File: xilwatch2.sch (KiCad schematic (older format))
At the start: 31 parts, among them J1 Conn_SWD, M1 Vibrator, Q1 NTR5103N, SW1 Btn_Up, SW2 Btn_Down, SW3 Btn_Select, SW4 Btn_Back, U1 ATSAMD21J18A-MU

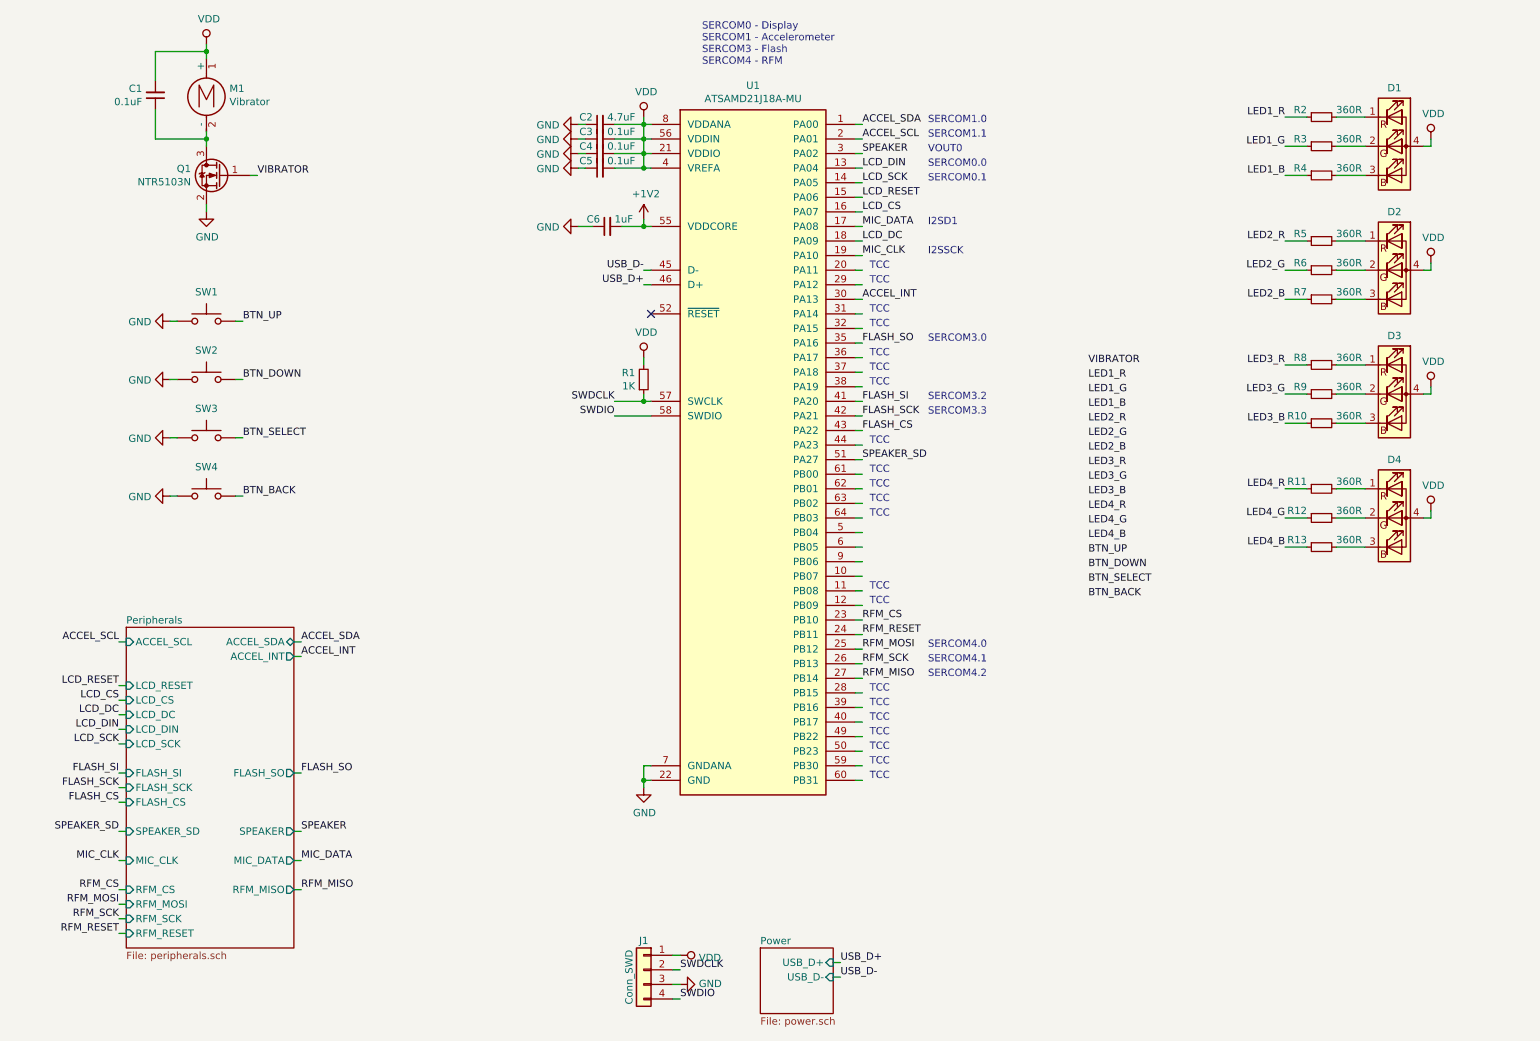
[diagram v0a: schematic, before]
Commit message: Change of plans, now a nRF52840 with E-ink
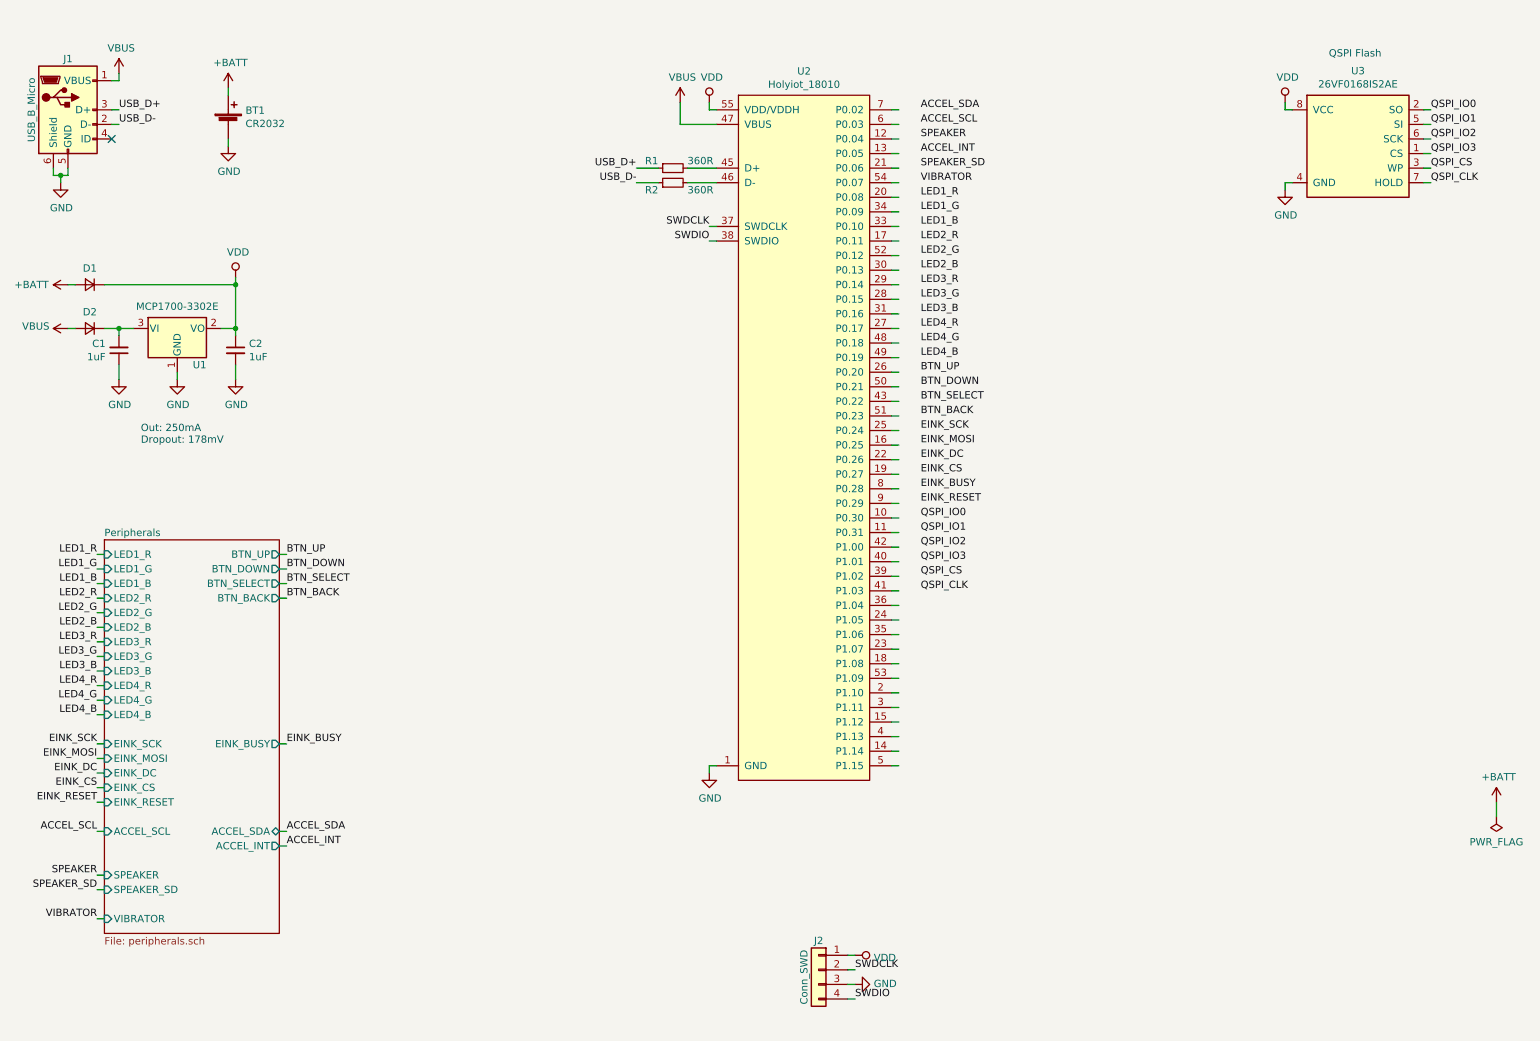
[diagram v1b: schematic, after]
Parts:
- removed C3, C4, C5: 0.1uF, Capacitor_SMD:C_0603_1608Metric, symbol Device:C_Small
- removed C6: 1uF, Capacitor_SMD:C_0603_1608Metric, symbol Device:C_Small
- removed D1: LED_TopLeft, LED_SMD_Extra:LED_RGBA_0606, symbol Device_Extra:LED_RGBA
- removed D2: LED_TopRight, LED_SMD_Extra:LED_RGBA_0606, symbol Device_Extra:LED_RGBA
- removed D3: LED_BottomLeft, LED_SMD_Extra:LED_RGBA_0606, symbol Device_Extra:LED_RGBA
- removed D4: LED_BottomRight, LED_SMD_Extra:LED_RGBA_0606, symbol Device_Extra:LED_RGBA
- removed M1: Vibrator, Buzzer_Beeper_Extra:C1026B, symbol Motor:Motor_DC
- removed Q1: NTR5103N, Package_TO_SOT_SMD:SOT-23, symbol Transistor_FET:BSS138
- removed R10, R11, R12, R13, R3, R4, R5, R6, R7, R8, R9: 360R, Resistor_SMD:R_0603_1608Metric, symbol Device:R_Small
- removed SW1: Btn_Up, Button_Switch_SMD_Extra:KLS7-TS2402, symbol Switch:SW_Push
- removed SW2: Btn_Down, Button_Switch_SMD_Extra:KLS7-TS2402, symbol Switch:SW_Push
- removed SW3: Btn_Select, Button_Switch_SMD_Extra:KLS7-TS2402, symbol Switch:SW_Push
- removed SW4: Btn_Back, Button_Switch_SMD_Extra:KLS7-TS2402, symbol Switch:SW_Push
- removed U1: ATSAMD21J18A-MU, Package_DFN_QFN:QFN-64-1EP_9x9mm_P0.5mm_EP4.7x4.7mm, symbol MCU_Microchip_SAMD:ATSAMD21J18A-MU
- added BT1: CR2032, Battery_Extra:BAT-HLD-001, symbol Device:Battery_Cell
- added D1, D2: S1JHE, Diode_SMD:D_SOD-323F, symbol Device:D_Small
- added J1: USB_B_Micro, Connector_USB:USB_Micro-B_Molex-105017-0001, symbol Connector:USB_B_Micro
- added U1: MCP1700-3302E, Package_TO_SOT_SMD:SOT-23, symbol Regulator_Linear:MCP1700-3302E_SOT23
- added U2: Holyiot_18010, RF_Module_Extra:Holyiot_18010, symbol RF_Bluetooth_Extra:Holyiot_18010
- added U3: 26VF0168IS2AE, Package_SON:WSON-8-1EP_6x5mm_P1.27mm_EP3.4x4mm, symbol Memory_Flash_Extra:26VF0168IS2AE
- C1: value 0.1uF -> 1uF
- C2: value 4.7uF -> 1uF
- R1: value 1K -> 360R
- renumbered J1 to J2
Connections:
- net labels added: +BATT, EINK_BUSY, EINK_CS, EINK_DC, EINK_MOSI, EINK_RESET, EINK_SCK, QSPI_CLK, QSPI_CS, QSPI_IO0, QSPI_IO1, QSPI_IO2, QSPI_IO3, VBUS
- net labels removed: +1V2, FLASH_CS, FLASH_SCK, FLASH_SI, FLASH_SO, LCD_CS, LCD_DC, LCD_DIN, LCD_RESET, LCD_SCK, MIC_CLK, MIC_DATA, RFM_CS, RFM_MISO, RFM_MOSI, RFM_RESET, RFM_SCK
- wire segments 154 -> 125
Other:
- note added: "Out: 250mA\nDropout: 178mV"
- note added: "QSPI Flash"
- note removed: "I2SD1"
- note removed: "I2SSCK"
- note removed: "SERCOM0 - Display\nSERCOM1 - Accelerometer\nSERCOM3 - Flash\nSERCOM4 - RFM"
- note removed: "SERCOM0.0"
- note removed: "SERCOM0.1"
- note removed: "SERCOM1.0"
- note removed: "SERCOM1.1"
- note removed: "SERCOM3.0"
- note removed: "SERCOM3.2\n"
- note removed: "SERCOM3.3"
- note removed: "SERCOM4.0\n"
- note removed: "SERCOM4.1"
- note removed: "SERCOM4.2"
- note removed: "TCC"
- note removed: "VOUT0"
- moved on the sheet: J2

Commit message: WIP
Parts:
- removed J2: Conn_SWD, Connector_JST:JST_SH_SM04B-SRSS-TB_1x04-1MP_P1.00mm_Horizontal, symbol Connector_Generic:Conn_01x04
- removed U3: 26VF0168IS2AE, Package_SON:WSON-8-1EP_6x5mm_P1.27mm_EP3.4x4mm, symbol Memory_Flash_Extra:26VF0168IS2AE
- added TP1: TP_GND, TestPoint:TestPoint_Pad_D1.0mm, symbol Connector:TestPoint
- added TP2: TP_VDD, TestPoint:TestPoint_Pad_D1.0mm, symbol Connector:TestPoint
- added TP3: TP_SWDCLK, TestPoint:TestPoint_Pad_D1.0mm, symbol Connector:TestPoint
- added TP4: TP_SWDIO, TestPoint:TestPoint_Pad_D1.0mm, symbol Connector:TestPoint
- added U3: IS25LP128F, Package_SON:WSON-8-1EP_6x5mm_P1.27mm_EP3.4x4mm, symbol Memory_Flash_Extra:IS25LP128F
- R1, R2: value 360R -> 22R
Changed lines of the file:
@@
 Comment4 ""
 $EndDescr
-$Comp
-L Connector_Generic:Conn_01x04 J2
-U 1 1 5BB51A34
-P 6200 7250
-F 0 "J2" H 6200 7450 50  0000 C CNN
-F 1 "Conn_SWD" V 6300 7200 50  0000 C CNN
-F 2 "Connector_JST:JST_SH_SM04B-SRSS-TB_1x04-1MP_P1.00mm_Horizontal" H 6200 7250 50  0001 C CNN
-F 3 "~" H 6200 7250 50  0001 C CNN
-	1    6200 7250
-	-1   0    0    -1
-$EndComp
-Wire Wire Line
-	6400 7150 6450 7150
-Wire Wire Line
-	6400 7250 6450 7250
-Wire Wire Line
-	6400 7350 6450 7350
-Wire Wire Line
-	6400 7450 6450 7450
+Wire Wire Line
+	6400 7600 6450 7600
+Wire Wire Line
+	6400 7300 6600 7300
+Wire Wire Line
+	6400 7500 6450 7500
+Wire Wire Line
+	6400 7400 6600 7400
 $Comp
 L power:VDD #PWR014
 U 1 1 5BB70814
-P 6450 7150
-F 0 "#PWR014" H 6450 7000 50  0001 C CNN
-F 1 "VDD" V 6467 7278 50  0000 L CNN
-F 2 "" H 6450 7150 50  0001 C CNN
-F 3 "" H 6450 7150 50  0001 C CNN
-	1    6450 7150
+P 6450 7600
+F 0 "#PWR014" H 6450 7450 50  0001 C CNN
+F 1 "VDD" V 6450 7750 50  0000 L CNN
+F 2 "" H 6450 7600 50  0001 C CNN
+F 3 "" H 6450 7600 50  0001 C CNN
+	1    6450 7600
 	0    1    1    0
 $EndComp
@@
 L power:GND #PWR015
 U 1 1 5BB70AB4
-P 6450 7350
-F 0 "#PWR015" H 6450 7100 50  0001 C CNN
-F 1 "GND" V 6455 7222 50  0000 R CNN
-F 2 "" H 6450 7350 50  0001 C CNN
-F 3 "" H 6450 7350 50  0001 C CNN
-	1    6450 7350
+P 6450 7500
+F 0 "#PWR015" H 6450 7250 50  0001 C CNN
+F 1 "GND" V 6450 7350 50  0000 R CNN
+F 2 "" H 6450 7500 50  0001 C CNN
+F 3 "" H 6450 7500 50  0001 C CNN
+	1    6450 7500
 	0    -1   -1   0
 $EndComp
-Text Label 6450 7250 0    50   ~ 0
+Text Label 6600 7300 0    50   ~ 0
 SWDCLK
-Text Label 6450 7450 0    50   ~ 0
+Text Label 6600 7400 0    50   ~ 0
 SWDIO
 $Bitmap
@@
 P 5200 1750
 F 0 "R1" V 5150 1850 50  0000 L CNN
-F 1 "360R" V 5150 1650 50  0000 R CNN
+F 1 "22R" V 5150 1650 50  0000 R CNN
 F 2 "Resistor_SMD:R_0603_1608Metric" H 5200 1750 50  0001 C CNN
 F 3 "~" H 5200 1750 50  0001 C CNN
@@
 P 5200 1850
 F 0 "R2" V 5150 1950 50  0000 L CNN
-F 1 "360R" V 5150 1750 50  0000 R CNN
+F 1 "22R" V 5150 1750 50  0000 R CNN
 F 2 "Resistor_SMD:R_0603_1608Metric" H 5200 1850 50  0001 C CNN
 F 3 "~" H 5200 1850 50  0001 C CNN
@@
 Text Label 6900 3950 0    50   ~ 0
 EINK_BUSY
-$Comp
-L Memory_Flash_Extra:26VF0168IS2AE U3
-U 1 1 5CE630DD
-P 9900 1600
-F 0 "U3" H 9900 2117 50  0000 C CNN
-F 1 "26VF0168IS2AE" H 9900 2026 50  0000 C CNN
-F 2 "Package_SON:WSON-8-1EP_6x5mm_P1.27mm_EP3.4x4mm" H 10400 1650 50  0001 C CNN
-F 3 "https://www.mouser.se/datasheet/2/268/25017A-709039.pdf" H 9900 1100 50  0001 C CNN
-	1    9900 1600
-	1    0    0    -1
-$EndComp
 Wire Wire Line
 	9450 1350 9400 1350
@@
 Text Label 1250 6100 2    50   ~ 0
 EINK_RESET
+$Comp
+L Memory_Flash_Extra:IS25LP128F U3
+U 1 1 5D2DFCAA
+P 9900 1600
+F 0 "U3" H 9900 2115 50  0000 C CNN
+F 1 "IS25LP128F" H 9900 2024 50  0000 C CNN
+F 2 "Package_SON:WSON-8-1EP_6x5mm_P1.27mm_EP3.4x4mm" H 9900 1100 50  0001 C CNN
+F 3 "https://www.mouser.se/datasheet/2/198/25LP-WP128F-1146765.pdf" H 9900 1000 50  0001 C CNN
+	1    9900 1600
+	1    0    0    -1
+$EndComp
+$Comp
+L Connector:TestPoint TP2
+U 1 1 5D305E20
+P 6400 7600
+F 0 "TP2" V 6400 7850 50  0000 C CNN
+F 1 "TP_VDD" V 6296 7674 50  0001 C CNN
+F 2 "TestPoint:TestPoint_Pad_D1.0mm" H 6600 7600 50  0001 C CNN
+F 3 "~" H 6600 7600 50  0001 C CNN
+	1    6400 7600
+	0    -1   1    0
+$EndComp
+$Comp
+L Connector:TestPoint TP3
+U 1 1 5D305EB4
+P 6400 7300
+F 0 "TP3" V 6400 7550 50  0000 C CNN
+F 1 "TP_SWDCLK" V 6296 7374 50  0001 C CNN
+F 2 "TestPoint:TestPoint_Pad_D1.0mm" H 6600 7300 50  0001 C CNN
+F 3 "~" H 6600 7300 50  0001 C CNN
+	1    6400 7300
+	0    -1   1    0
+$EndComp
+$Comp
+L Connector:TestPoint TP1
+U 1 1 5D305EE2
+P 6400 7500
+F 0 "TP1" V 6400 7750 50  0000 C CNN
+F 1 "TP_GND" V 6296 7574 50  0001 C CNN
+F 2 "TestPoint:TestPoint_Pad_D1.0mm" H 6600 7500 50  0001 C CNN
+F 3 "~" H 6600 7500 50  0001 C CNN
+	1    6400 7500
+	0    -1   1    0
+$EndComp
+$Comp
+L Connector:TestPoint TP4
+U 1 1 5D305F0E
+P 6400 7400
+F 0 "TP4" V 6400 7650 50  0000 C CNN
+F 1 "TP_SWDIO" V 6296 7474 50  0001 C CNN
+F 2 "TestPoint:TestPoint_Pad_D1.0mm" H 6600 7400 50  0001 C CNN
+F 3 "~" H 6600 7400 50  0001 C CNN
+	1    6400 7400
+	0    -1   1    0
+$EndComp
 $EndSCHEMATC
